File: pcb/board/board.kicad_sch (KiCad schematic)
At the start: 20 parts, among them J1 USB_C_Receptacle_USB2.0, J3 Micro_SD_Card_Det, J4 Conn_01x05_Male, J6 Conn_02x02_Top_Bottom

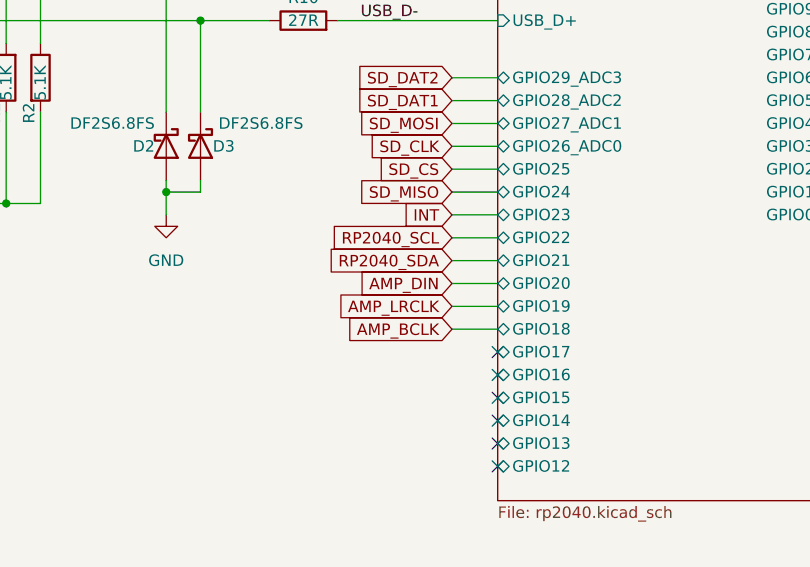
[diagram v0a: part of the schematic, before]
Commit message: Update readmes. Uncovered I2C bug :(
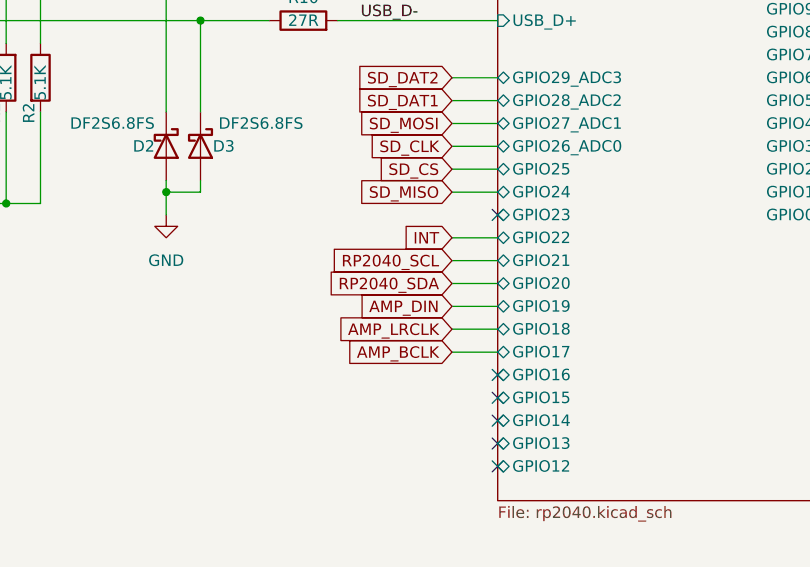
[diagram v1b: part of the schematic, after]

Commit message: Update readme and pcb
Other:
- moved on the sheet: D1, D2, D3, J1, J4, J6, R1, R10, R2, R9

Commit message: pcb version 0.3
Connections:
- net SD_DAT1: no longer names the net of J3.8 (DAT1), R3.2
- net SD_DAT2: no longer names the net of J3.1 (DAT2), R8.2
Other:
- sheet Power ports: added BAT_V_SENSE, CHG_EN; removed none
